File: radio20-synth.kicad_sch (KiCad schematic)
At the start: 0 parts

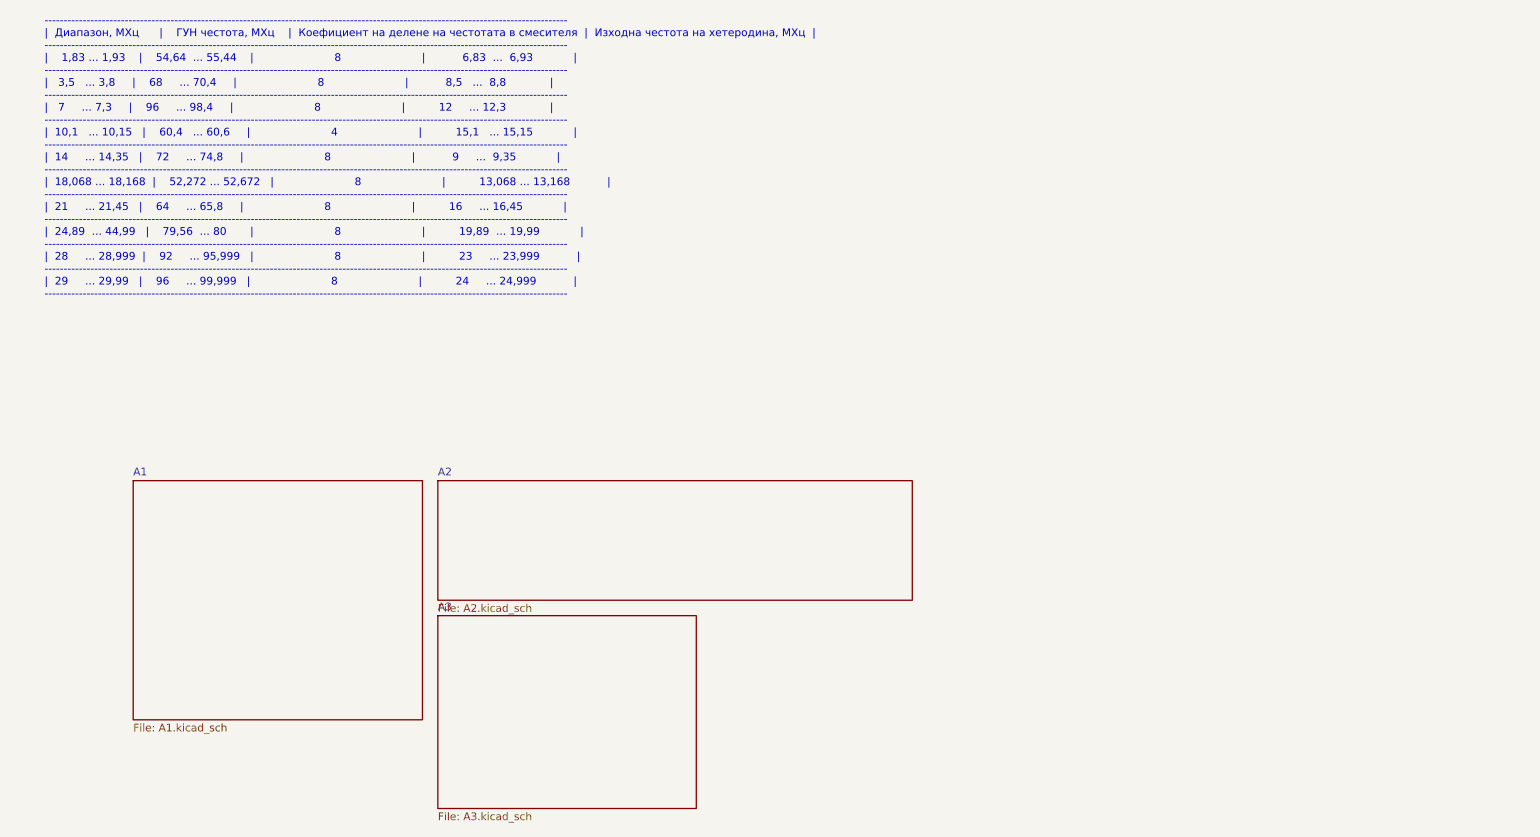
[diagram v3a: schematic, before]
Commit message: Update to kicad7; flush WIP
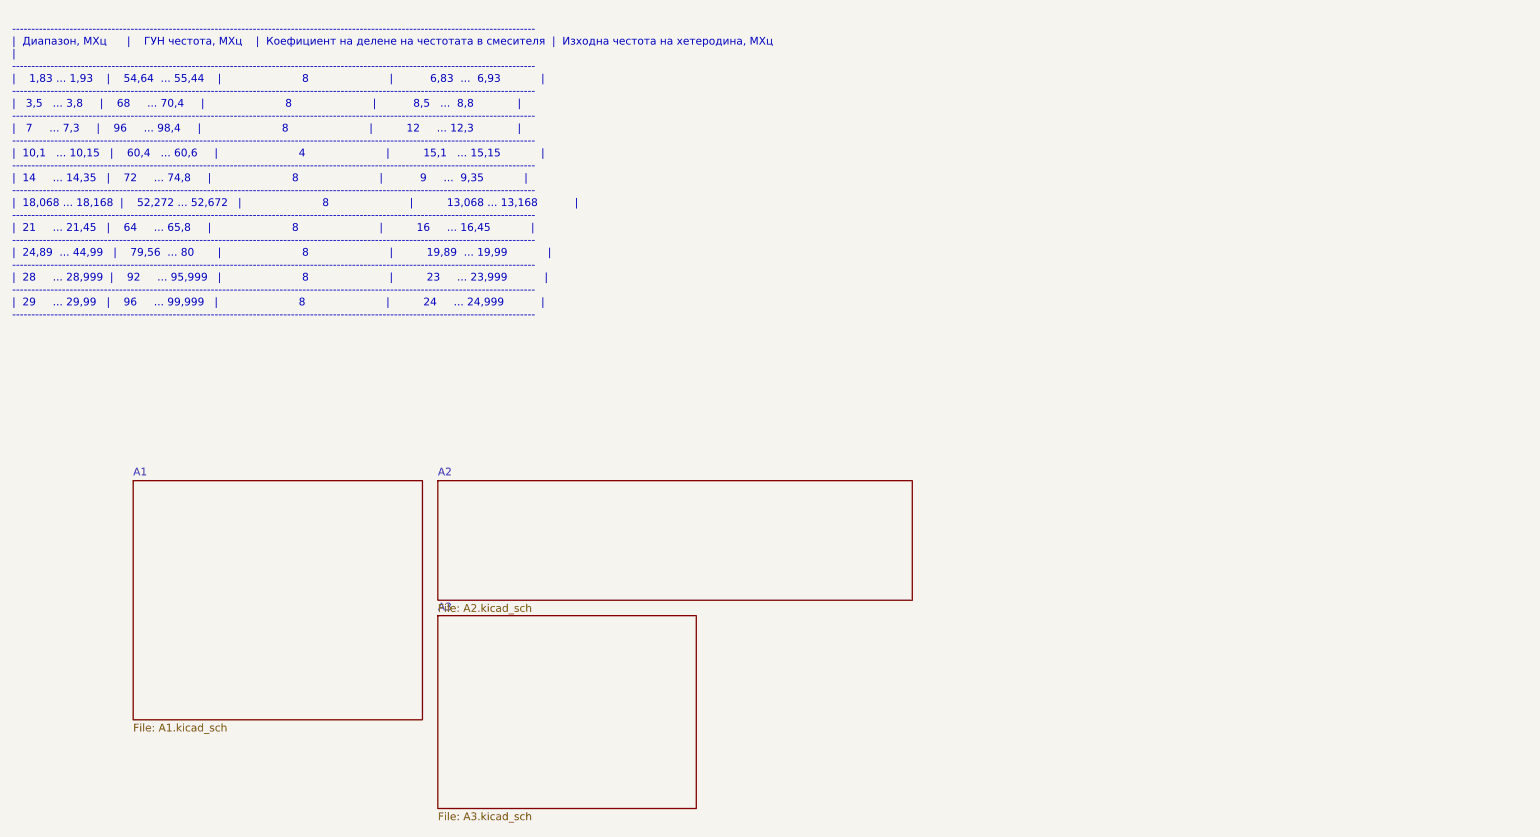
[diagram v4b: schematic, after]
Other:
- note removed: "----------------------------------------------------------------------------------------------------------------------------------------- | Диапазон, МХц | ГУН честота, МХц | Коефициент на делене на честотата в смесителя | Изходна честота на хетеродина, МХц | ----------------------------------------------------------------------------------------------------------------------------------------- |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"
